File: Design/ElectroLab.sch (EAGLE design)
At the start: 232 parts, among them IC1 LM2902DT, IC10 CD4511BNSR, IC11 PAM8403, IC13 ADXL337, IC14 MIC5205, IC2 LM2902DT, IC3 SN74LV08ADR, IC4 SN74LV32ADR, IC5 SN74LV04ADR, IC6 4027D, IC7 4027D, IC8 NE555D, P1 SLIDE_POT_20MM, P2 ALPS_RK09K_VERTICAL, P3 ALPS_RK09K_VERTICAL, U1 USB, U2 GAS_SENSOR

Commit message: Updated V3R1
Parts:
- removed AR1, AR2, AR3, AR4: 1K, SpaceDIY:RESISTOR_ARRAY_X8_CAY17
- removed C33, C34: 10uF, SpaceDIY_passive_components:C0603
- removed D1, D2, D3, D4: (no value), Seeed-OPL-Diode:SMD-DIODE-SWITCHING-75V-150MA(D1206)
- removed DP1: 2X7_SEGMENT_COMMON_CATODE_12_PINS, SpaceDIY:2X7_SEGMENT_COMMON_CATODE_12_PINS
- removed IC1, IC2: LM2902DT, Texas Instruments_By_element14_Batch_1:LM2902DT
- removed IC10: CD4511BNSR, SpaceDIY:SN74LS247D
- removed IC5: SN74LV04ADR, Texas Instruments_By_element14_Batch_1:SN74LV04ADR
- removed JC1, JC2: SWTCHCRFT_3.5JACK5-JACK-SMD, jmsaavedra:SWTCHCRFT_3.5JACK5-JACK-SMD
- removed L0, L1, L2, L3, L4, L5, L6, L7: (no value), adafruit:LEDSMT1206
- removed L10, L17, L8, L9: Grn, adafruit:LEDSMT1206
- removed L11, L12, L13: Ylw, adafruit:LEDSMT1206
- removed L14, L15, L16: Red, adafruit:LEDSMT1206
- removed LDR: V1060_21, photo-elements:V1060_21
- removed LED_: LED_RGB_PLCC-6, SpaceDIY_passive_components:LED_RGB_PLCC-6
- removed PB1, PB2, PB3, PB4, PB5, PB6, PB7, PB8, PB9: SMD-SWITCH-TACTILE-SPST-NO/TS-1109(4P-D6.0MM), Seeed-OPL-Switch:SMD-SWITCH-TACTILE-SPST-NO/TS-1109(4P-D6.0MM)
- removed PH10, PH2, PH21, PH3, PH4, PH5, PH6, PH7, PH8, PH9: (no value), pinhead:PINHD-1X2
- removed PH11, PH14, PH15, PH16, PH17, PH18, PH19, PH20, PH22, PH23, PH24, PH25, PH26, PH27, PH28, PH29, PH30, PH38, PH64: (no value), pinhead:PINHD-1X3
- removed PH31, PH58, PH59, PH60, PH61, PH62: (no value), pinhead:PINHD-1X30
- removed PH32, PH33, PH35, PH36, PH37, PH65: (no value), pinhead:PINHD-1X4
- removed PH34: (no value), pinhead:PINHD-1X1
- removed PH39, PH40: (no value), pinhead:PINHD-1X6
- removed PH41: (no value), pinhead:PINHD-2X7
- removed PH42, PH43, PH44, PH45, PH46: (no value), pinhead:PINHD-1X8
- removed PH47: (no value), pinhead:PINHD-1X9
- removed PH48, PH49, PH50, PH51, PH52, PH53, PH54, PH55, PH56, PH57: PINHD-1X10, adafruit:PINHD-1X10
- removed PH63: (no value), con-lstb:MA08-2
- added ARR1, ARR2, ARR3, ARR4, ARR5, ARR6, ARR7: 4_RES_ARRAY_R06031KOHM, SpaceDIY_passive_components:4_RES_ARRAY_R06031KOHM
- added C28, C37, C38, C39: 10uF, rcl:C-USC0603
- added D5, D6, D7, D8: LL4148, SpaceDIY_semiconductors:LL4148
- added IC15: 74HC32S14-13, SpaceDIY_IC:74AHC32DD
- added IC9: TP4056, TP4056:TP4056
- added J1: (no value), SpaceDIY_connectors:BAT_CONN-JST-2MM-SMT
- added J10, J11, J12, J2, J4, J5, J6, J7, J8, J9: (no value), SpaceDIY_connectors:CONN_10"
- added J13: AUDIO_JACK_MONO_3.5LCSC, SpaceDIY_connectors:AUDIO_JACK_MONO_3.5LCSC
- added J14, J15, J16, J17, J18, J19: (no value), SpaceDIY_connectors:CONN_30
- added J20, J21, J22, J23, J24, J25, J26, J27, J28, J29, J30, J31, J32, J33, J34, J35, J36, J37: (no value), SpaceDIY_connectors:CONN_03
- added J3, J43, J44, J52, J53, J55: (no value), SpaceDIY_connectors:CONN_04
- added J38, J39, J40, J41, J47, J48, J49, J50, J54: (no value), SpaceDIY_connectors:CONN_02
- added J42, J51: (no value), SpaceDIY_connectors:CONN_01
- added J45, J46: (no value), SpaceDIY_connectors:CONN_06
- added J56: (no value), SpaceDIY_connectors:CONN_09
- added LED1, LED10, LED11, LED12, LED13, LED2, LED3, LED4, LED5, LED6, LED7, LED8, LED9: E6CC1205RYGC2UDA, SpaceDIY_semiconductors:RED&GREEN_LED
- added RGB: CLEAR, SpaceDIY_semiconductors:LED-RGB-CCCLEAR
- added S10, S2, S3, S4, S5, S6, S7, S8, S9: MOMENTARY-SWITCH-SPST-PTH-6.0MM, SparkFun-Switches:MOMENTARY-SWITCH-SPST-PTH-6.0MM
- added U$1: FJ5101AG, SpaceDIY_semiconductors:7-SEGMENT-1DIGIT-GREEN
- added U$2, U$3, U$4, U$5, U$6: CONN_08, SpaceDIY_connectors:CONN_08
- added U$7: CD4511BNSR, SpaceDIY_IC:CD4511BNSR
- added U3: AMS1117-3.3VSMD, SpaceDIY_IC:AMS1117-3.3VSMD
- added X8: USB-C-POWER, SpaceDIY_connectors:USB-C-POWER
- C1, C10, C11, C12, C13, C14, C15, C16, C2, C3, C4, C5, C6, C7, C8, C9: device resistor:C-USC1206 -> SpaceDIY_passive_components:C0603
- C17, C18: device rcl:CPOL-USA/3216-18R -> SpaceDIY_passive_components:C3528; LCSC (none) -> C16133
- C19, C20, C35, C36: device rcl:CPOL-USD/7343-31R -> SpaceDIY_passive_components:C7343
- C27: device rcl:CPOL-USD/7343-31W -> SpaceDIY_passive_components:C7343; LCSC (none) -> C7229
- C29, C30, C31: value 10nF -> 0.1uF
- C32: value 100nF -> 0.1uF
- F1: LCSC (none) -> C355568
- IC13: value ADXL337 -> 74HC08DD; device SpaceDIY_IC:ADXL337 -> SpaceDIY_IC:74HC08DD
- IC14: value MIC5205 -> 74HC04DD; device SparkFun:V_REG_LDOSMD -> SpaceDIY_IC:74HC04DD
- IC3: value SN74LV08ADR -> LM324DTD; device Texas Instruments_By_element14_Batch_1:SN74LVC08AD -> SpaceDIY_IC:LM324DTD
- IC4: value SN74LV32ADR -> LM324DTD; device Texas Instruments_By_element14_Batch_1:SN74S32D -> SpaceDIY_IC:LM324DTD
- IC6, IC7: value 4027D -> MC74HC112ADR2G; device 40xx:4027D -> SpaceDIY_IC:JK_FLIP_FLOPMC74HC112ADR2G
- IC8: value NE555D -> TLC555CDR; LCSC (none) -> C6986
- MIC: value ELECTRET_MICROPHON-WM-64PC/64PK -> MICROPHONE; device microphon:ELECTRET_MICROPHON-WM-64PC/64PK -> SpaceDIY_sensors:MICROPHONE
- NTC: device adafruit:R-US_R1206 -> SpaceDIY_sensors:THERMISTOR
- P1: device SpaceDIY:SLIDE_POT_20MM -> SpaceDIY_electromechanical:SLIDE_POT_20MM
- PH1: value (none) -> PHOTORESISTOR; device pinhead:PINHD-1X1 -> SpaceDIY_sensors:PHOTORESISTOR
- PH12: device pinhead:PINHD-1X3 -> SpaceDIY_connectors:CONN_03
- R1, R10, R11, R12, R13, R14, R15, R16, R17, R18, R19, R2, R20, R21, R22, R23, R24, R25, R26, R27, R28, R29, R3, R30, R31, R35, R36, R37, R38, R39, R4, R41, R42, R43, R44, R45, R46, R47, R48, R49, R5, R50, R51, R52, R53, R54, R55, R56, R57, R58, R59, R6, R7, R8, R9: device resistor:R-US_R1206 -> SpaceDIY_passive_components:R0603
- R32: value 330 -> 1.2k; device resistor:R-US_R1206 -> rcl:R-US_R0603
- R33: value 330 -> 1K; device resistor:R-US_R1206 -> SpaceDIY_passive_components:R0603
- R34: value 330 -> 1k; device resistor:R-US_R1206 -> SpaceDIY_passive_components:R0603
- SP1: value 32MM_SPEAKER -> SPEAKERFS1508MB0810-H8.0; device SpaceDIY:32MM_SPEAKER -> SpaceDIY_electromechanical:SPEAKERFS1508MB0810-H8.0
- T1: value (none) -> MMBT2222A; device transistor:BC817-16-NPN-SOT23-BEC -> SpaceDIY_semiconductors:T_NPNMMBT2222A-1P_CHANGJ_SOT23-BEC
- T2, T3: value (none) -> T_NPNMMBT2222A-1P_CHANGJ_SOT23-BEC; device transistor:BC817-16-NPN-SOT23-BEC -> SpaceDIY_semiconductors:T_NPNMMBT2222A-1P_CHANGJ_SOT23-BEC
- T4, T5: value (none) -> T_PNPMMBT5401_CHANGJ_SOT23-BEC; device transistor:-PNP-SOT23-BCE -> SpaceDIY_semiconductors:T_PNPMMBT5401_CHANGJ_SOT23-BEC
- U$16: device SpaceDIY:RESISTIVE_SENSOR_PAD -> SpaceDIY_sensors:RESISTIVE_SENSOR_PAD
- U1: value USB -> ADXL335; device daspilker:USB-RECEPTABLE -> SparkFun-Sensors:ADXL335; LCSC (none) -> C34439
- U2: device SparkFun:GAS_SENSOR -> SpaceDIY_sensors:GAS_SENSORMQ-3
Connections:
- removed net 3.3V: C32.1, C33.1, IC13.VS@1, IC13.VS@2, IC14.OUT
- removed net D0: PH41.1, PH63.1, R32.2
- removed net D1: PH41.2, PH63.2
- removed net D10: PH41.11, PH63.11, R37.2
- removed net D11: PH41.12, PH63.12
- removed net D12: PH41.13, PH63.13, R38.2
- removed net D13: PH41.14, PH63.14
- removed net D2: PH41.3, PH63.3, R33.2
- removed net D3: PH41.4, PH63.4
- removed net D4: PH41.5, PH63.5, R34.2
- removed net D5: PH41.6, PH63.6
- removed net D6: PH41.7, PH63.7, R35.2
- removed net D7: PH41.8, PH63.8
- removed net D8: PH41.9, PH63.9, R36.2
- removed net D9: PH41.10, PH63.10
- removed net DG1: DP1.9, PH3.1
- removed net DG2: DP1.4, PH3.2
- removed net DP: DP1.2
- removed net JC1: JC1.2, PH12.2
- removed net JC2: JC2.2, PH64.2
- removed net N$121: JC2.3, PH64.1
- removed net N$228: PB1.A0, PB1.A1, PB2.A0, PB2.A1, PB3.A0, PB3.A1, PH19.3
- removed net N$229: PB4.A0, PB4.A1, PB5.A0, PB5.A1, PB6.A0, PB6.A1, PH19.2
- removed net N$230: PB7.A0, PB7.A1, PB8.A0, PB8.A1, PB9.A0, PB9.A1, PH19.1
- removed net N$233: PB3.B0, PB3.B1, PB6.B0, PB6.B1, PB9.B0, PB9.B1, PH20.3
- removed net N$292: L8.A, R48.1
- removed net N$300: L9.A, R49.1
- removed net N$301: L10.A, R50.1
- removed net N$302: L11.A, R51.1
- removed net N$303: L12.A, R52.1
- removed net N$304: L13.A, R53.1
- removed net N$305: L14.A, R54.1
- removed net N$306: L15.A, R55.1
- removed net N$307: L16.A, R56.1
- removed net VEXT: PH63.15, S1.L1
- removed net VUSB: S1.L2, U1.VCC
- new net N$182: LED5-G.C, R49.2
- new net N$185: LED6-G.C, R50.2
- new net N$204: LED7-G.C, R51.2
- new net N$214: LED8-G.C, R52.2
- new net N$215: LED9-G.C, R53.2
- new net N$216: LED7-R.C, R35.2
- new net N$246: LED8-R.C, R36.2
- new net N$247: LED9-R.C, R37.2
- new net N$248: LED10-R.C, R54.2
- new net N$251: LED11-R.C, R55.2
- new net N$252: LED12-R.C, R56.2
- new net N$253: J20.3, S2.1, S3.1, S4.1
- new net N$258: J20.2, S5.1, S6.1, S7.1
- new net N$260: J21.3, S10.2, S4.2, S7.2
- new net N$261: J20.1, S10.1, S8.1, S9.1
- new net VBAT: C28.1, IC9.BAT, J1.+, S1.R1
- new net VIN: C37.1, IC9.CE, IC9.VCC, LED1-G.A, LED1-R.A, R38.2, U2.A1, U2.H1, X8.VBUS
- new net VOUT: C39.1, F1.2, U3.OUT
- net A1A: now also ARR1_1.1, IC13.1A, U$2.1; no longer AR1.9, IC3.1A, PH45.1
- net A1B: now also ARR1_2.1, IC13.1B, U$2.2; no longer AR1.8, IC3.1B, PH45.2
- net A1Y: now also IC13.1Y, J52.1; no longer IC3.1Y, PH36.1
- net A2A: now also ARR1_3.1, IC13.2A, U$2.3; no longer AR1.7, IC3.2A, PH45.3
- net A2B: now also ARR1_4.1, IC13.2B, U$2.4; no longer AR1.6, IC3.2B, PH45.4
- net A2Y: now also IC13.2Y, J52.2; no longer IC3.2Y, PH36.2
- net A3A: now also ARR2_1.1, IC13.3A, U$2.5; no longer AR1.1, IC3.3A, PH45.5
- net A3B: now also ARR2_2.1, IC13.3B, U$2.6; no longer AR1.2, IC3.3B, PH45.6
- net A3Y: now also IC13.3Y, J52.3; no longer IC3.3Y, PH36.3
- net A4A: now also ARR2_3.1, IC13.4A, U$2.7; no longer AR1.3, IC3.4A, PH45.7
- net A4B: now also ARR2_4.1, IC13.4B, U$2.8; no longer AR1.4, IC3.4B, PH45.8
- net A4Y: now also IC13.4Y, J52.4; no longer IC3.4Y, PH36.4
- net B: now also J37.3; no longer PH11.3
- net G: now also J37.2, R58.2; no longer PH11.2, R57.2
- net GND: now also ARR1_1.2, ARR1_2.2, ARR1_3.2, ARR1_4.2, ARR2_1.2, ARR2_2.2, ARR2_3.2, ARR2_4.2, ARR3_1.2, ARR3_2.2, ARR3_3.2, ARR3_4.2, ARR4_1.2, ARR4_2.2, ARR4_3.2, ARR4_4.2, ARR5_1.2, ARR5_2.2, ARR5_3.2, ARR5_4.2, ARR6_1.2, ARR6_2.2, ARR7_1.2, ARR7_2.2, ARR7_3.2, ARR7_4.2, C28.2, C37.2, C38.2, C39.2, IC13.GND, IC15.GND, IC9.GND, IC9.TEMP, J1.-, J14.1, J14.10, J14.11, J14.12, J14.13, J14.14, J14.15, J14.16, J14.17, J14.18, J14.19, J14.2, J14.20, J14.21, J14.22, J14.23, J14.24, J14.25, J14.26, J14.27, J14.28, J14.29, J14.3, J14.30, J14.4, J14.5, J14.6, J14.7, J14.8, J14.9, J36.1, LED13-G.C, LED2-G.C, LED3-G.C, R32.1, R35.1, R36.1, R37.1, R48.1, R49.1, R50.1, R51.1, R52.1, R53.1, R54.1, R55.1, R56.1, RGB.C, U$1.G1, U$1.G2, U$7.GND, U$7.LE, U1.COM@3, U1.COM@5, U1.COM@6, U1.COM@7, U3.GND, X8.GND; no longer AR1.10, AR1.5, AR2.10, AR2.5, AR3.10, AR3.5, AR4.10, AR4.5, C33.2, C34.2, IC1.GND, IC10.GND, IC10.RBI, IC13.GND@1, IC13.GND@2, IC2.GND, IC5.GND, L0.C, L1.C, L10.C, L11.C, L12.C, L13.C, L14.C, L15.C, L16.C, L17.C, L2.C, L3.C, L4.C, L5.C, L6.C, L7.C, L8.C, L9.C, LED_B.C, LED_G.C, LED_R.C, PH38.1, PH62.1, PH62.10, PH62.11, PH62.12, PH62.13, PH62.14, PH62.15, PH62.16, PH62.17, PH62.18, PH62.19, PH62.2, PH62.20, PH62.21, PH62.22, PH62.23, PH62.24, PH62.25, PH62.26, PH62.27, PH62.28, PH62.29, PH62.3, PH62.30, PH62.4, PH62.5, PH62.6, PH62.7, PH62.8, PH62.9, PH63.16, U1.GND
- net I1A: now also ARR5_1.1, IC14.1A, J45.1; no longer AR3.9, IC5.1A, PH39.1
- net I1Y: now also IC14.1Y, J46.1; no longer IC5.1Y, PH40.1
- net I2A: now also ARR5_2.1, IC14.2A, J45.2; no longer AR3.3, IC5.2A, PH39.2
- net I2Y: now also IC14.2Y, J46.2; no longer IC5.2Y, PH40.2
- net I3A: now also ARR5_3.1, IC14.3A, J45.3; no longer AR3.7, IC5.3A, PH39.3
- net I3Y: now also IC14.3Y, J46.3; no longer IC5.3Y, PH40.3
- net I4A: now also ARR5_4.1, IC14.4A, J45.4; no longer AR3.6, IC5.4A, PH39.4
- net I4Y: now also IC14.4Y, J46.4; no longer IC5.4Y, PH40.4
- net I5A: now also ARR6_1.1, IC14.5A, J45.5; no longer AR3.1, IC5.5A, PH39.5
- net I5Y: now also IC14.5Y, J46.5; no longer IC5.5Y, PH40.5
- net I6A: now also ARR6_2.1, IC14.6A, J45.6; no longer AR3.2, IC5.6A, PH39.6
- net I6Y: now also IC14.6Y, J46.6; no longer IC5.6Y, PH40.6
- net IA: now also ARR7_1.1, J55.1, U$7.IA; no longer AR4.9, IC10.IA, PH35.1
- net IB: now also ARR7_2.1, J55.2, U$7.IB; no longer AR4.8, IC10.IB, PH35.2
- net IC: now also ARR7_3.1, J55.3, U$7.IC; no longer AR4.7, IC10.IC, PH35.3
- net ID: now also ARR7_4.1, J55.4, U$7.ID; no longer AR4.6, IC10.ID, PH35.4
- net IN_L: now also J36.3; no longer PH38.3
- net IN_R: now also J36.2; no longer PH38.2
- net L1: now also J56.1, LED4-G.A; no longer PH47.9, R48.2
- net L2: now also J56.2, LED5-G.A; no longer PH47.8, R49.2
- net L3: now also J56.3, LED6-G.A; no longer PH47.7, R50.2
- net L4: now also J56.4, LED7-G.A, LED7-R.A; no longer PH47.6, R51.2
- net L5: now also J56.5, LED8-G.A, LED8-R.A; no longer PH47.5, R52.2
- net L6: now also J56.6, LED9-G.A, LED9-R.A; no longer PH47.4, R53.2
- net L7: now also J56.7, LED10-R.A; no longer PH47.3, R54.2
- net L8: now also J56.8, LED11-R.A; no longer PH47.2, R55.2
- net L9: now also J56.9, LED12-R.A; no longer PH47.1, R56.2
- net N$1: now also J2.1; no longer PH48.10
- net N$10: now also J2.10; no longer PH48.1
- net N$100: now also J12.1; no longer PH55.1
- net N$101: now also D8.A, J53.4; no longer D4.+, PH32.4
- net N$102: now also J13.2, PH12.2; no longer L1.A, R32.1
- net N$103: now also LED2-G.A; no longer L0.A
- net N$104: now also IC9.!STDBY, R34.2; no longer L2.A, R33.1
- net N$105: now also LED1-R.C, R33.1; no longer L3.A, R34.1
- net N$106: now also LED1-G.C, R34.1; no longer L4.A, R35.1
- net N$107: now also IC9.PROG, R32.2; no longer L5.A, R36.1
- net N$108: now also IC9.!CHRG, R33.2; no longer L6.A, R37.1
- net N$109: now also C38.1, S1.RC, U3.IN; no longer L7.A, R38.1
- net N$11: now also J4.10; no longer PH49.10
- net N$110: now also D8.C, J44.4; no longer D4.-, PH33.4
- net N$111: now also D5.A, J53.1; no longer D1.+, PH32.1
- net N$112: now also J47.1; no longer PH9.2
- net N$113: now also J48.1; no longer PH7.2
- net N$114: now also J49.1; no longer PH10.2
- net N$115: now also J50.1; no longer PH8.2
- net N$116: now also J13.1; no longer JC1.3
- net N$117: now also RGB.G; no longer LED_G.A
- net N$118: now also LED4-G.C, R48.2; no longer F1.1, S1.LC
- net N$119: now also J42.1; no longer PH34.1
- net N$12: now also J4.9; no longer PH49.9
- net N$120: now also LED13-G.A, R38.1; no longer JC2.1, PH64.3
- net N$122: now also LED3-G.A; no longer L17.A
- net N$125: now also J41.2; no longer PH21.1
- net N$126: now also J41.1; no longer PH21.2
- net N$127: now also J15.24, J16.24, J17.24, J18.24; no longer PH31.7, PH59.7, PH60.7, PH61.7
- net N$128: now also J15.30, J16.30, J17.30, J18.30; no longer PH31.1, PH59.1, PH60.1, PH61.1
- net N$129: now also J15.29, J16.29, J17.29, J18.29; no longer PH31.2, PH59.2, PH60.2, PH61.2
- net N$13: now also J4.8; no longer PH49.8
- net N$130: now also IC3.1+, U$4.1; no longer IC1.4IN-, PH42.1
- net N$131: now also IC3.1-, U$4.2; no longer IC1.4IN+, PH42.2
- net N$132: now also IC3.2+, U$4.3; no longer IC1.3IN-, PH42.3
- net N$133: now also IC3.2-, U$4.4; no longer IC1.3IN+, PH42.4
- net N$134: now also IC3.3+, U$4.5; no longer IC1.2IN-, PH42.5
- net N$135: now also IC3.3-, U$4.6; no longer IC1.2IN+, PH42.6
- net N$136: now also IC3.4+, U$4.7; no longer IC1.1IN-, PH42.7
- net N$137: now also IC3.4-, U$4.8; no longer IC1.1IN+, PH42.8
- net N$138: now also IC4.1+, U$5.1; no longer IC2.4IN-, PH43.1
- net N$139: now also J15.28, J16.28, J17.28, J18.28; no longer PH31.3, PH59.3, PH60.3, PH61.3
- net N$14: now also J4.7; no longer PH49.7
- net N$140: now also J15.27, J16.27, J17.27, J18.27; no longer PH31.4, PH59.4, PH60.4, PH61.4
- net N$141: now also J15.26, J16.26, J17.26, J18.26; no longer PH31.5, PH59.5, PH60.5, PH61.5
- net N$142: now also J15.25, J16.25, J17.25, J18.25; no longer PH31.6, PH59.6, PH60.6, PH61.6
- net N$143: now also J15.23, J16.23, J17.23, J18.23; no longer PH31.8, PH59.8, PH60.8, PH61.8
- net N$144: now also J15.22, J16.22, J17.22, J18.22; no longer PH31.9, PH59.9, PH60.9, PH61.9
- net N$145: now also J15.21, J16.21, J17.21, J18.21; no longer PH31.10, PH59.10, PH60.10, PH61.10
- net N$146: now also J26.1; no longer PH27.1
- net N$147: now also J15.20, J16.20, J17.20, J18.20; no longer PH31.11, PH59.11, PH60.11, PH61.11
- net N$148: now also J15.19, J16.19, J17.19, J18.19; no longer PH31.12, PH59.12, PH60.12, PH61.12
- net N$149: now also J15.18, J16.18, J17.18, J18.18; no longer PH31.13, PH59.13, PH60.13, PH61.13
- net N$15: now also J4.5; no longer PH49.5
- net N$150: now also J15.17, J16.17, J17.17, J18.17; no longer PH31.14, PH59.14, PH60.14, PH61.14
- net N$151: now also J15.16, J16.16, J17.16, J18.16; no longer PH31.15, PH59.15, PH60.15, PH61.15
- net N$152: now also J15.15, J16.15, J17.15, J18.15; no longer PH31.16, PH59.16, PH60.16, PH61.16
- net N$153: now also J15.14, J16.14, J17.14, J18.14; no longer PH31.17, PH59.17, PH60.17, PH61.17
- net N$154: now also J15.13, J16.13, J17.13, J18.13; no longer PH31.18, PH59.18, PH60.18, PH61.18
- net N$155: now also J26.2; no longer PH27.2
- net N$156: now also J26.3; no longer PH27.3
- net N$157: now also J27.1; no longer PH25.1
- net N$158: now also J27.2; no longer PH25.2
- net N$159: now also J27.3; no longer PH25.3
- net N$16: now also J4.6; no longer PH49.6
- net N$160: now also J28.1; no longer PH28.1
- net N$161: now also J28.2; no longer PH28.2
- net N$162: now also J28.3; no longer PH28.3
- net N$163: now also J15.12, J16.12, J17.12, J18.12; no longer PH31.19, PH59.19, PH60.19, PH61.19
- net N$164: now also J15.11, J16.11, J17.11, J18.11; no longer PH31.20, PH59.20, PH60.20, PH61.20
- net N$165: now also J15.10, J16.10, J17.10, J18.10; no longer PH31.21, PH59.21, PH60.21, PH61.21
- net N$166: now also J15.9, J16.9, J17.9, J18.9; no longer PH31.22, PH59.22, PH60.22, PH61.22
- net N$167: now also J15.8, J16.8, J17.8, J18.8; no longer PH31.23, PH59.23, PH60.23, PH61.23
- net N$168: now also J15.7, J16.7, J17.7, J18.7; no longer PH31.24, PH59.24, PH60.24, PH61.24
- net N$169: now also J15.6, J16.6, J17.6, J18.6; no longer PH31.25, PH59.25, PH60.25, PH61.25
- net N$17: now also J4.4; no longer PH49.4
- net N$170: now also J15.5, J16.5, J17.5, J18.5; no longer PH31.26, PH59.26, PH60.26, PH61.26
- net N$171: now also J29.1; no longer PH26.1
- net N$172: now also J29.2; no longer PH26.2
- net N$173: now also J29.3; no longer PH26.3
- net N$174: now also J15.4, J16.4, J17.4, J18.4; no longer PH31.27, PH59.27, PH60.27, PH61.27
- net N$175: now also J15.3, J16.3, J17.3, J18.3; no longer PH31.28, PH59.28, PH60.28, PH61.28
- net N$176: now also J15.2, J16.2, J17.2, J18.2; no longer PH31.29, PH59.29, PH60.29, PH61.29
- net N$177: now also J15.1, J16.1, J17.1, J18.1; no longer PH31.30, PH59.30, PH60.30, PH61.30
- net N$178: now also J47.2; no longer PH9.1
- net N$179: now also J48.2; no longer PH7.1
- net N$18: now also J4.3; no longer PH49.3
- net N$180: now also J49.2; no longer PH10.1
- net N$181: now also J50.2; no longer PH8.1
- net N$183: now also D7.A, J53.3; no longer D3.+, PH32.3
- net N$184: now also D6.A, J53.2; no longer D2.+, PH32.2
- net N$186: now also IC4.1-, U$5.2; no longer IC2.4IN+, PH43.2
- net N$187: now also IC4.2+, U$5.3; no longer IC2.3IN-, PH43.3
- net N$188: now also IC4.2-, U$5.4; no longer IC2.3IN+, PH43.4
- net N$189: now also IC4.3+, U$5.5; no longer IC2.2IN-, PH43.5
- net N$19: now also J4.2; no longer PH49.2
- net N$190: now also IC4.3-, U$5.6; no longer IC2.2IN+, PH43.6
- net N$191: now also IC4.4+, U$5.7; no longer IC2.1IN-, PH43.7
- net N$192: now also IC4.4-, U$5.8; no longer IC2.1IN+, PH43.8
- net N$193: now also IC3.1Y, U$6.1; no longer IC1.4OUT, PH44.8
- net N$194: now also IC3.2Y, U$6.2; no longer IC1.3OUT, PH44.7
- net N$195: now also IC3.3Y, U$6.3; no longer IC1.2OUT, PH44.6
- net N$196: now also IC3.4Y, U$6.4; no longer IC1.1OUT, PH44.5
- net N$197: now also IC4.1Y, U$6.5; no longer IC2.4OUT, PH44.4
- net N$198: now also IC4.2Y, U$6.6; no longer IC2.3OUT, PH44.3
- net N$199: now also D5.C, J44.1; no longer D1.-, PH33.1
- net N$2: now also J2.2; no longer PH48.9
- net N$20: now also J4.1; no longer PH49.1
- net N$200: now also IC4.3Y, U$6.7; no longer IC2.2OUT, PH44.2
- net N$201: now also IC4.4Y, U$6.8; no longer IC2.1OUT, PH44.1
- net N$202: now also D6.C, J44.2; no longer D2.-, PH33.2
- net N$203: now also D7.C, J44.3; no longer D3.-, PH33.3
- net N$205: now also J31.1; no longer PH16.1
- net N$206: now also J31.2; no longer PH16.2
- net N$207: now also J31.3; no longer PH16.3
- net N$208: now also J32.1; no longer PH17.1
- net N$209: now also J32.2; no longer PH17.2
- net N$21: now also J5.1; no longer PH50.10
- net N$210: now also J32.3; no longer PH17.3
- net N$211: now also J33.1; no longer PH18.1
- net N$212: now also J33.2; no longer PH18.2
- net N$213: now also J33.3; no longer PH18.3
- net N$217: now also J34.1; no longer PH14.1
- net N$218: now also J34.2; no longer PH14.2
- net N$219: now also J34.3; no longer PH14.3
- net N$22: now also J5.2; no longer PH50.9
- net N$220: now also J35.1; no longer PH15.1
- net N$221: now also J35.2; no longer PH15.2
- net N$222: now also J35.3; no longer PH15.3
- net N$223: now also J30.1; no longer PH29.1
- net N$224: now also J51.1; no longer PH1.1
- net N$226: now also J30.2; no longer PH29.2
- net N$227: now also J30.3; no longer PH29.3
- net N$23: now also J5.3; no longer PH50.8
- net N$231: now also J21.1, S2.2, S5.2, S8.2; no longer PB1.B0, PB1.B1, PB4.B0, PB4.B1, PB7.B0, PB7.B1, PH20.1
- net N$232: now also J21.2, S3.2, S6.2, S9.2; no longer PB2.B0, PB2.B1, PB5.B0, PB5.B1, PB8.B0, PB8.B1, PH20.2
- net N$234: now also J39.1, PH1.1; no longer LDR.1, PH5.1
- net N$235: now also J39.2, PH1.3; no longer LDR.2, PH5.2
- net N$236: now also J40.1; no longer PH6.1
- net N$237: now also J23.1; no longer PH22.1
- net N$238: now also J23.2; no longer PH22.2
- net N$239: now also J23.3; no longer PH22.3
- net N$24: now also J5.4; no longer PH50.7
- net N$240: now also J22.1; no longer PH24.1
- net N$241: now also J22.2; no longer PH24.2
- net N$242: now also J22.3; no longer PH24.3
- net N$243: now also J24.1; no longer PH23.1
- net N$244: now also J24.2; no longer PH23.2
- net N$245: now also J24.3; no longer PH23.3
- net N$249: now also J38.1; no longer PH4.1
- net N$25: now also J5.5; no longer PH50.6
- net N$250: now also J38.2; no longer PH4.2
- net N$256: now also J40.2; no longer PH6.2
- net N$257: now also J54.2; no longer PH2.1
- net N$26: now also J5.6; no longer PH50.5
- net N$264: now also J13.3; no longer JC1.1
- net N$27: now also J5.7; no longer PH50.4
- net N$28: now also J5.8; no longer PH50.3
- net N$29: now also J5.9; no longer PH50.2
- net N$291: now also J54.1; no longer PH2.2
- net N$3: now also J2.3; no longer PH48.8
- net N$30: now also J5.10; no longer PH50.1
- net N$308: now also RGB.R; no longer LED_R.A
- net N$31: now also J6.10; no longer PH51.10
- net N$310: now also RGB.B; no longer LED_B.A
- net N$32: now also J6.9; no longer PH51.9
- net N$33: now also J6.8; no longer PH51.8
- net N$34: now also J6.7; no longer PH51.7
- net N$35: now also J6.6; no longer PH51.6
- net N$36: now also J6.5; no longer PH51.5
- net N$37: now also J6.4; no longer PH51.4
- net N$38: now also J6.3; no longer PH51.3
- net N$39: now also J6.2; no longer PH51.2
- net N$4: now also J2.4; no longer PH48.7
- net N$40: now also J6.1; no longer PH51.1
- net N$41: now also J7.1; no longer PH52.10
- net N$42: now also J7.2; no longer PH52.9
- net N$43: now also J7.3; no longer PH52.8
- net N$44: now also J7.4; no longer PH52.7
- net N$45: now also J7.5; no longer PH52.6
- net N$46: now also J7.6; no longer PH52.5
- net N$47: now also J7.7; no longer PH52.4
- net N$48: now also J7.8; no longer PH52.3
- net N$49: now also J7.9; no longer PH52.2
- net N$5: now also J2.5; no longer PH48.6
- net N$50: now also J7.10; no longer PH52.1
- net N$51: now also J8.10; no longer PH53.10
- net N$52: now also J8.9; no longer PH53.9
- net N$53: now also J8.8; no longer PH53.8
- net N$54: now also J8.7; no longer PH53.7
- net N$55: now also J8.6; no longer PH53.6
- net N$56: now also J8.5; no longer PH53.5
- net N$57: now also J8.4; no longer PH53.4
- net N$58: now also J8.3; no longer PH53.3
- net N$59: now also J8.2; no longer PH53.2
- net N$6: now also J2.6; no longer PH48.5
- net N$60: now also J8.1; no longer PH53.1
- net N$61: now also J9.1; no longer PH56.10
- net N$62: now also J9.2; no longer PH56.9
- net N$63: now also J9.3; no longer PH56.8
- net N$64: now also J9.4; no longer PH56.7
- net N$65: now also J9.5; no longer PH56.6
- net N$66: now also J9.6; no longer PH56.5
- net N$67: now also J9.7; no longer PH56.4
- net N$68: now also J9.8; no longer PH56.3
- net N$69: now also J9.9; no longer PH56.2
- net N$7: now also J2.7; no longer PH48.4
- net N$70: now also J9.10; no longer PH56.1
- net N$71: now also J10.1; no longer PH57.1
- net N$72: now also J10.2; no longer PH57.2
- net N$73: now also J10.3; no longer PH57.3
- net N$74: now also J10.4; no longer PH57.4
- net N$75: now also J10.5; no longer PH57.5
- net N$76: now also J10.6; no longer PH57.6
- net N$77: now also J10.7; no longer PH57.7
- net N$78: now also J10.8; no longer PH57.8
- net N$79: now also J10.9; no longer PH57.9
- net N$8: now also J2.8; no longer PH48.3
- net N$80: now also J10.10; no longer PH57.10
- net N$81: now also J11.1; no longer PH54.10
- net N$82: now also J11.2; no longer PH54.9
- net N$83: now also J11.3; no longer PH54.8
- net N$84: now also J11.4; no longer PH54.7
- net N$85: now also J11.5; no longer PH54.6
- net N$86: now also J11.6; no longer PH54.5
- net N$87: now also J11.7; no longer PH54.4
- net N$88: now also J11.8; no longer PH54.3
- net N$89: now also J11.9; no longer PH54.2
- net N$9: now also J2.9; no longer PH48.2
- net N$90: now also J11.10; no longer PH54.1
- net N$91: now also J12.10; no longer PH55.10
- net N$92: now also J12.9; no longer PH55.9
- net N$93: now also J12.8; no longer PH55.8
- net N$94: now also J12.7; no longer PH55.7
- net N$95: now also J12.6; no longer PH55.6
- net N$96: now also J12.5; no longer PH55.5
- net N$97: now also J12.4; no longer PH55.4
- net N$98: now also J12.3; no longer PH55.3
- net N$99: now also J12.2; no longer PH55.2
- net O1A: now also ARR3_1.1, IC15.1A, U$3.1; no longer AR2.9, IC4.1A, PH46.1
- net O1B: now also ARR3_2.1, IC15.1B, U$3.2; no longer AR2.8, IC4.1B, PH46.2
- net O1Y: now also IC15.1Y, J43.1; no longer IC4.1Y, PH37.1
- net O2A: now also ARR3_3.1, IC15.2A, U$3.3; no longer AR2.7, IC4.2A, PH46.3
- net O2B: now also ARR3_4.1, IC15.2B, U$3.4; no longer AR2.6, IC4.2B, PH46.4
- net O2Y: now also IC15.2Y, J43.2; no longer IC4.2Y, PH37.2
- net O3A: now also ARR4_1.1, IC15.3A, U$3.5; no longer AR2.1, IC4.3A, PH46.5
- net O3B: now also ARR4_2.1, IC15.3B, U$3.6; no longer AR2.2, IC4.3B, PH46.6
- net O3Y: now also IC15.3Y, J43.3; no longer IC4.3Y, PH37.3
- net O4A: now also ARR4_3.1, IC15.4A, U$3.7; no longer AR2.3, IC4.4A, PH46.7
- net O4B: now also ARR4_4.1, IC15.4B, U$3.8; no longer AR2.4, IC4.4B, PH46.8
- net O4Y: now also IC15.4Y, J43.4; no longer IC4.4Y, PH37.4
- net OUT_L+: now also J3.1; no longer PH65.4
- net OUT_L-: now also J3.2; no longer PH65.3
- net OUT_R+: now also J3.3; no longer PH65.2
- net OUT_R-: now also J3.4; no longer PH65.1
- net R: now also J37.1, R57.2; no longer PH11.1, R58.2
- net SA: now also U$1.A; no longer DP1.10
- net SA': now also U$7.A; no longer IC10.A
- net SB: now also U$1.B; no longer DP1.8
- net SB': now also U$7.B; no longer IC10.B
- net SC: now also U$1.C; no longer DP1.1
- net SC': now also U$7.C; no longer IC10.C
- net SD: now also U$1.D; no longer DP1.5
- net SD': now also U$7.D; no longer IC10.D
- net SE: now also U$1.E; no longer DP1.3
- net SE': now also U$7.E; no longer IC10.E
- net SF: now also U$1.F; no longer DP1.6
- net SF': now also U$7.F; no longer IC10.F
- net SG: now also U$1.G; no longer DP1.7
- net SG': now also U$7.G; no longer IC10.G
- net VCC: now also C32.1, F1.1, IC13.VCC, IC14.VCC, IC15.VCC, J19.1, J19.10, J19.11, J19.12, J19.13, J19.14, J19.15, J19.16, J19.17, J19.18, J19.19, J19.2, J19.20, J19.21, J19.22, J19.23, J19.24, J19.25, J19.26, J19.27, J19.28, J19.29, J19.3, J19.30, J19.4, J19.5, J19.6, J19.7, J19.8, J19.9, U$7.!BL, U$7.!LT, U$7.VCC, U1.VS@14, U1.VS@15; no longer C34.1, F1.2, IC1.VCC, IC10.BI/RBO, IC10.LT, IC10.VCC, IC14.EN, IC14.IN, IC2.VCC, IC5.VCC, PH58.1, PH58.10, PH58.11, PH58.12, PH58.13, PH58.14, PH58.15, PH58.16, PH58.17, PH58.18, PH58.19, PH58.2, PH58.20, PH58.21, PH58.22, PH58.23, PH58.24, PH58.25, PH58.26, PH58.27, PH58.28, PH58.29, PH58.3, PH58.30, PH58.4, PH58.5, PH58.6, PH58.7, PH58.8, PH58.9, U2.A1, U2.H1
- net X+: now also J25.1, U1.XOUT; no longer IC13.XOUT, PH30.1
- net Y+: now also J25.2, U1.YOUT; no longer IC13.YOUT, PH30.2
- net Z+: now also J25.3, U1.ZOUT; no longer IC13.ZOUT, PH30.3
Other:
- note added: "R4 [k] - IBAT [mA] ------------------------ 10 - 130 5 - 250 4 - 300 3 - 400 2 - 580 1.66 - 690 1.5 - 780 1.33 - 900 1.2 - 1000"
- note removed: "Aux Interface"

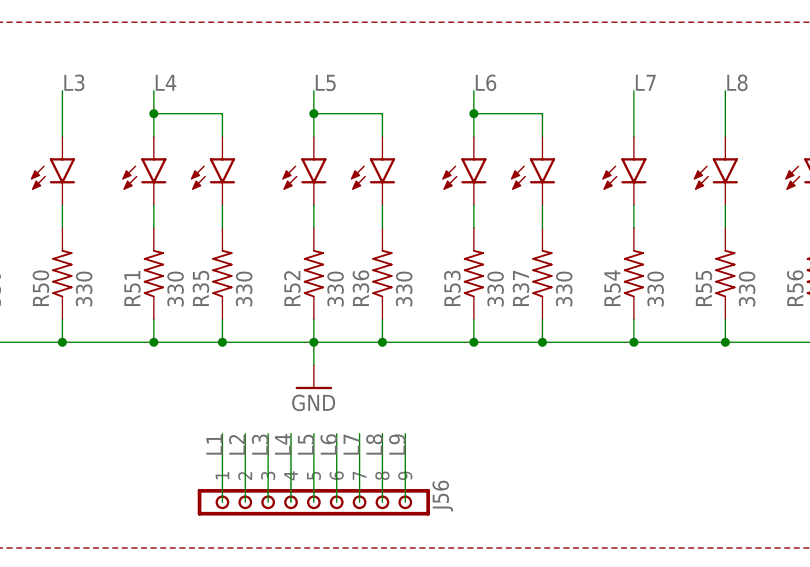
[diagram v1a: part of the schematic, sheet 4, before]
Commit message: V3 fixed: - USB-C - BCD pinhead - 330 -> 470 Ohm on RED LEDs for orange led bards
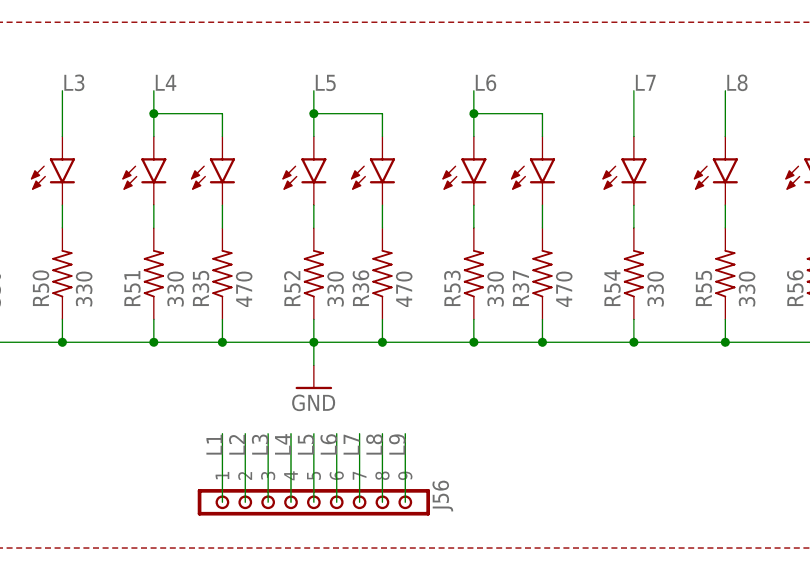
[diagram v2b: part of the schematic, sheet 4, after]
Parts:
- R35, R36, R37: value 330 -> 470
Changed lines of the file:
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@@
 <part name="LED11" library="SpaceDIY_semiconductors" deviceset="RED&amp;GREEN_LED" device="" value="E6CC1205RYGC2UDA"/>
 <part name="LED12" library="SpaceDIY_semiconductors" deviceset="RED&amp;GREEN_LED" device="" value="E6CC1205RYGC2UDA"/>
-<part name="R35" library="SpaceDIY_passive_components" deviceset="R0603" device="" value="330"/>
-<part name="R36" library="SpaceDIY_passive_components" deviceset="R0603" device="" value="330"/>
-<part name="R37" library="SpaceDIY_passive_components" deviceset="R0603" device="" value="330"/>
+<part name="R35" library="SpaceDIY_passive_components" deviceset="R0603" device="" value="470"/>
+<part name="R36" library="SpaceDIY_passive_components" deviceset="R0603" device="" value="470"/>
+<part name="R37" library="SpaceDIY_passive_components" deviceset="R0603" device="" value="470"/>
 <part name="RGB" library="SpaceDIY_semiconductors" deviceset="LED-RGB-CC" device="CLEAR" value="CLEAR"/>
 <part name="U1" library="SparkFun-Sensors" deviceset="ADXL335" device="">

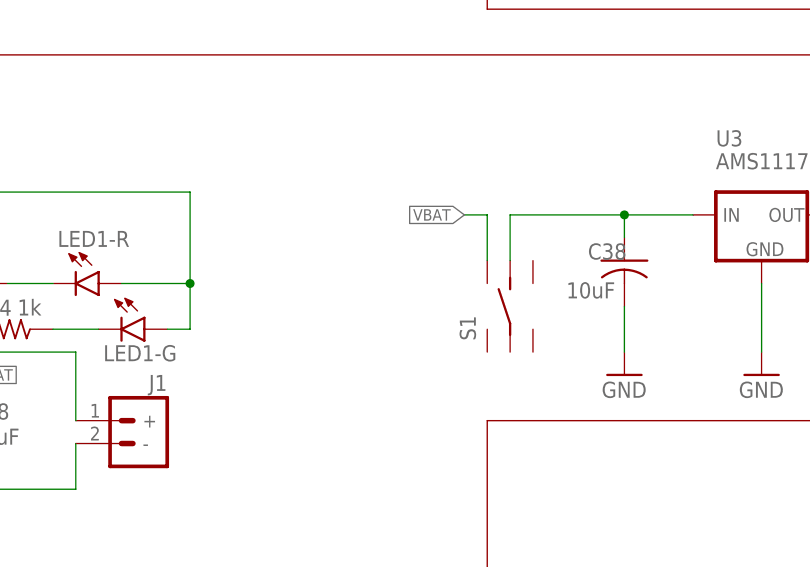
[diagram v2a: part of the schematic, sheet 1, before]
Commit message: Replaced Jack connector MQ-2 sensor power through main switch
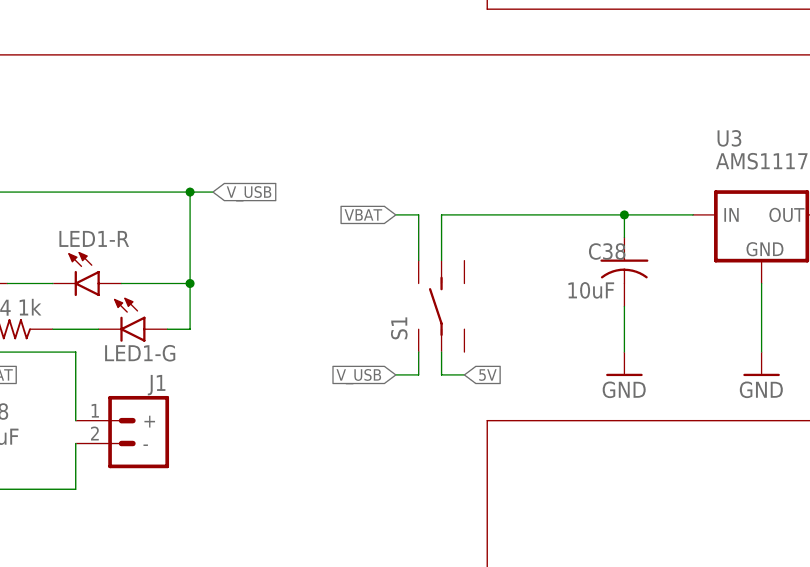
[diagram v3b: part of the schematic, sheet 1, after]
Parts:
- removed J13: AUDIO_JACK_MONO_3.5LCSC, SpaceDIY_connectors:AUDIO_JACK_MONO_3.5LCSC
- added JACK: AUDIO_JACK_MONO_3.5_3P, SpaceDIY_connectors:AUDIO_JACK_MONO_3.5_3P
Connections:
- removed net VIN: C37.1, IC9.CE, IC9.VCC, LED1-G.A, LED1-R.A, R38.2, U2.A1, U2.H1, X8.VBUS
- new net 5V: R38.2, S1.LC, U2.A1, U2.H1
- new net V_USB: C37.1, IC9.CE, IC9.VCC, LED1-G.A, LED1-R.A, S1.L1, X8.VBUS
- net N$102: now also JACK.2; no longer J13.2
- net N$116: now also JACK.1; no longer J13.1
- net N$264: now also JACK.3; no longer J13.3
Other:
- moved on the sheet: S1
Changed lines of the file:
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@@
 <part name="U2" library="SpaceDIY_sensors" deviceset="GAS_SENSOR" device="" technology="MQ-3" value="GAS_SENSOR"/>
 <part name="R67" library="SpaceDIY_passive_components" deviceset="R0603" device="" value="10k"/>
-<part name="P+1" library="SparkFun" deviceset="3.3V" device="" value="VUSB"/>
+<part name="P+1" library="SparkFun" deviceset="3.3V" device="" value="5V"/>
 <part name="GND1" library="SparkFun" deviceset="GND" device=""/>
 <part name="R39" library="SpaceDIY_passive_components" deviceset="R0603" device="" value="330"/>
@@
 <part name="J11" library="SpaceDIY_connectors" deviceset="CONN_10" device="&quot;"/>
 <part name="J12" library="SpaceDIY_connectors" deviceset="CONN_10" device="&quot;"/>
-<part name="J13" library="SpaceDIY_connectors" deviceset="AUDIO_JACK_MONO_3.5" device="LCSC"/>
 <part name="J14" library="SpaceDIY_connectors" deviceset="CONN_30" device=""/>
 <part name="J15" library="SpaceDIY_connectors" deviceset="CONN_30" device=""/>
@@
 <part name="LED13" library="SpaceDIY_semiconductors" deviceset="RED&amp;GREEN_LED" device="" value="E6CC1205RYGC2UDA"/>
 <part name="PH1" library="SpaceDIY_sensors" deviceset="PHOTORESISTOR" device=""/>
+<part name="JACK" library="SpaceDIY_connectors" deviceset="AUDIO_JACK_MONO_3.5_3P" device=""/>
 </parts>
 <sheets>
@@
 <attribute name="VALUE" x="227.711" y="87.376" size="1.778" layer="96" rot="R90"/>
 </instance>
-<instance part="S1" gate="G$1" x="154.94" y="40.64" smashed="yes" rot="R90">
-<attribute name="NAME" x="151.13" y="36.83" size="1.778" layer="95" rot="R90"/>
-<attribute name="VALUE" x="160.02" y="36.83" size="1.778" layer="96" rot="R90"/>
+<instance part="S1" gate="G$1" x="147.32" y="40.64" smashed="yes" rot="R90">
+<attribute name="NAME" x="143.51" y="36.83" size="1.778" layer="95" rot="R90"/>
+<attribute name="VALUE" x="152.4" y="36.83" size="1.778" layer="96" rot="R90"/>
 </instance>
 <instance part="R31" gate="G$1" x="220.98" y="50.8" smashed="yes">
@@
 </segment>
 <segment>
-<wire x1="152.4" y1="50.8" x2="149.86" y2="50.8" width="0.1524" layer="91"/>
-<label x="149.86" y="50.8" size="1.27" layer="95" rot="R180" xref="yes"/>
+<wire x1="144.78" y1="50.8" x2="142.24" y2="50.8" width="0.1524" layer="91"/>
+<label x="142.24" y="50.8" size="1.27" layer="95" rot="R180" xref="yes"/>
 <pinref part="S1" gate="G$1" pin="R1"/>
-<wire x1="152.4" y1="45.72" x2="152.4" y2="50.8" width="0.1524" layer="91"/>
+<wire x1="144.78" y1="45.72" x2="144.78" y2="50.8" width="0.1524" layer="91"/>
 </segment>
 </net>
@@
 </segment>
 </net>
-<net name="VIN" class="0">
+<net name="V_USB" class="0">
 <segment>
 <wire x1="53.34" y1="53.34" x2="86.36" y2="53.34" width="0.1524" layer="91"/>
@@
 <pinref part="LED1" gate="-R" pin="A"/>
 <pinref part="LED1" gate="-G" pin="A"/>
+<label x="121.92" y="53.34" size="1.27" layer="95" xref="yes"/>
+<wire x1="119.38" y1="53.34" x2="121.92" y2="53.34" width="0.1524" layer="91"/>
+<junction x="119.38" y="53.34"/>
+</segment>
+<segment>
+<pinref part="S1" gate="G$1" pin="L1"/>
+<wire x1="144.78" y1="35.56" x2="144.78" y2="33.02" width="0.1524" layer="91"/>
+<wire x1="144.78" y1="33.02" x2="142.24" y2="33.02" width="0.1524" layer="91"/>
+<label x="142.24" y="33.02" size="1.27" layer="95" rot="R180" xref="yes"/>
 </segment>
 </net>
@@
 <segment>
 <wire x1="175.26" y1="50.8" x2="167.64" y2="50.8" width="0.1524" layer="91"/>
-<wire x1="167.64" y1="50.8" x2="154.94" y2="50.8" width="0.1524" layer="91"/>
-<wire x1="154.94" y1="50.8" x2="154.94" y2="45.72" width="0.1524" layer="91"/>
+<wire x1="167.64" y1="50.8" x2="147.32" y2="50.8" width="0.1524" layer="91"/>
+<wire x1="147.32" y1="50.8" x2="147.32" y2="45.72" width="0.1524" layer="91"/>
 <pinref part="S1" gate="G$1" pin="RC"/>
 <pinref part="U3" gate="G$1" pin="IN"/>
@@
 </segment>
 </net>
+<net name="5V" class="0">
+<segment>
+<pinref part="S1" gate="G$1" pin="LC"/>
+<wire x1="147.32" y1="35.56" x2="147.32" y2="33.02" width="0.1524" layer="91"/>
+<wire x1="147.32" y1="33.02" x2="149.86" y2="33.02" width="0.1524" layer="91"/>
+<label x="149.86" y="33.02" size="1.27" layer="95" xref="yes"/>
+</segment>
+</net>
 </nets>
 </sheet>
@@
 </segment>
 </net>
-<net name="VIN" class="0">
+<net name="5V" class="0">
 <segment>
 <pinref part="U2" gate="G$1" pin="A1"/>
@@
 <attribute name="VALUE" x="178.562" y="92.71" size="1.778" layer="96" rot="R90"/>
 </instance>
-<instance part="J13" gate="G$1" x="228.6" y="154.94" smashed="yes" rot="R180"/>
 <instance part="J36" gate="G$1" x="147.32" y="144.78" smashed="yes">
 <attribute name="VALUE" x="144.78" y="142.494" size="1.778" layer="96"/>
@@
 <attribute name="VALUE" x="30.48" y="109.22" size="1.778" layer="96"/>
 </instance>
+<instance part="JACK" gate="G$1" x="228.6" y="154.94" smashed="yes" rot="R180"/>
 </instances>
 <busses>
@@
 <wire x1="208.28" y1="152.4" x2="200.66" y2="152.4" width="0.1524" layer="91"/>
 <pinref part="PH12" gate="G$1" pin="3"/>
-<pinref part="J13" gate="G$1" pin="3"/>
+<pinref part="JACK" gate="G$1" pin="3"/>
 </segment>
 </net>
@@
 <pinref part="PH12" gate="G$1" pin="1"/>
 <wire x1="200.66" y1="147.32" x2="218.44" y2="147.32" width="0.1524" layer="91"/>
-<pinref part="J13" gate="G$1" pin="1"/>
+<pinref part="JACK" gate="G$1" pin="1"/>
 </segment>
 </net>
@@
 <pinref part="PH12" gate="G$1" pin="2"/>
 <wire x1="213.36" y1="149.86" x2="213.36" y2="152.4" width="0.1524" layer="91"/>
-<pinref part="J13" gate="G$1" pin="2"/>
+<pinref part="JACK" gate="G$1" pin="2"/>
 </segment>
 </net>
